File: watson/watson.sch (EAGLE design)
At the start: 37 parts

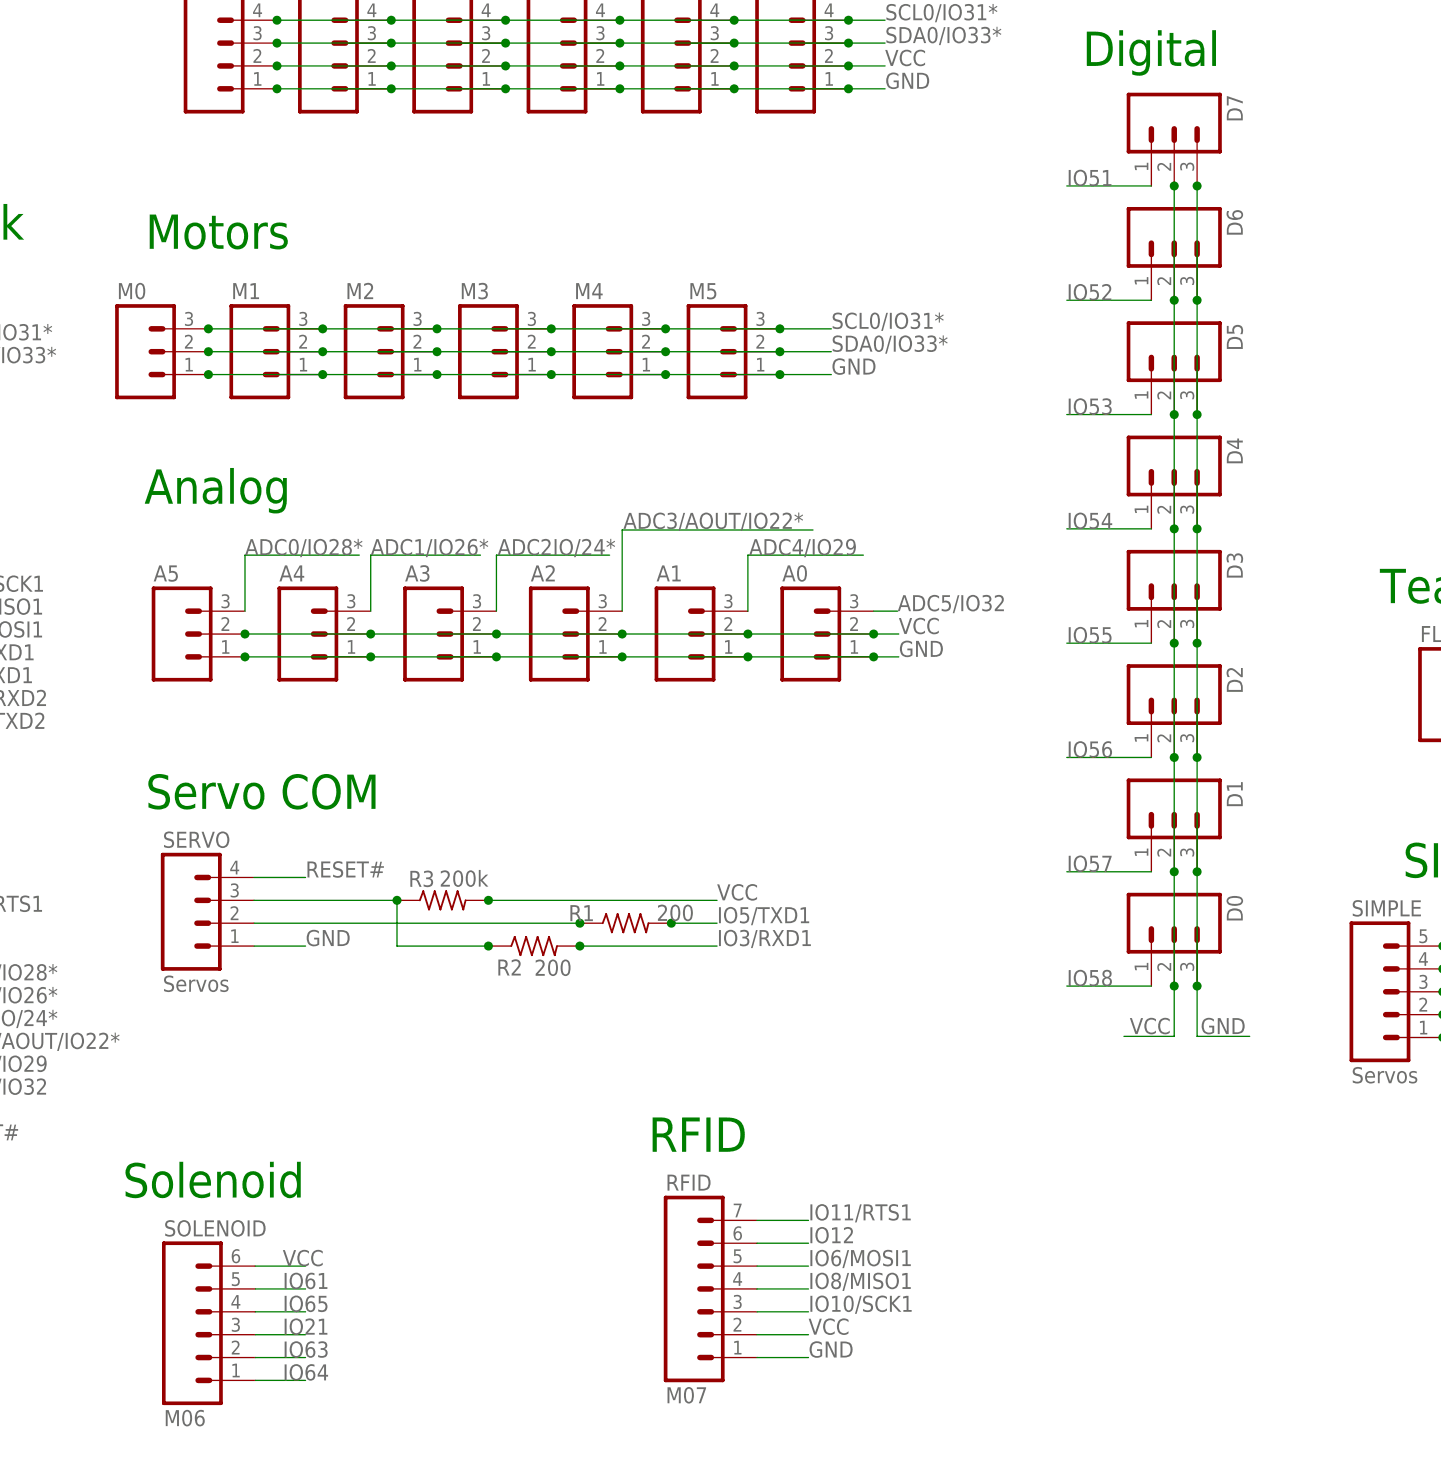
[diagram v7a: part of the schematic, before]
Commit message: Watson changes
holes aligned
silkscreen
gnd consistent
solenoid connected
etc.
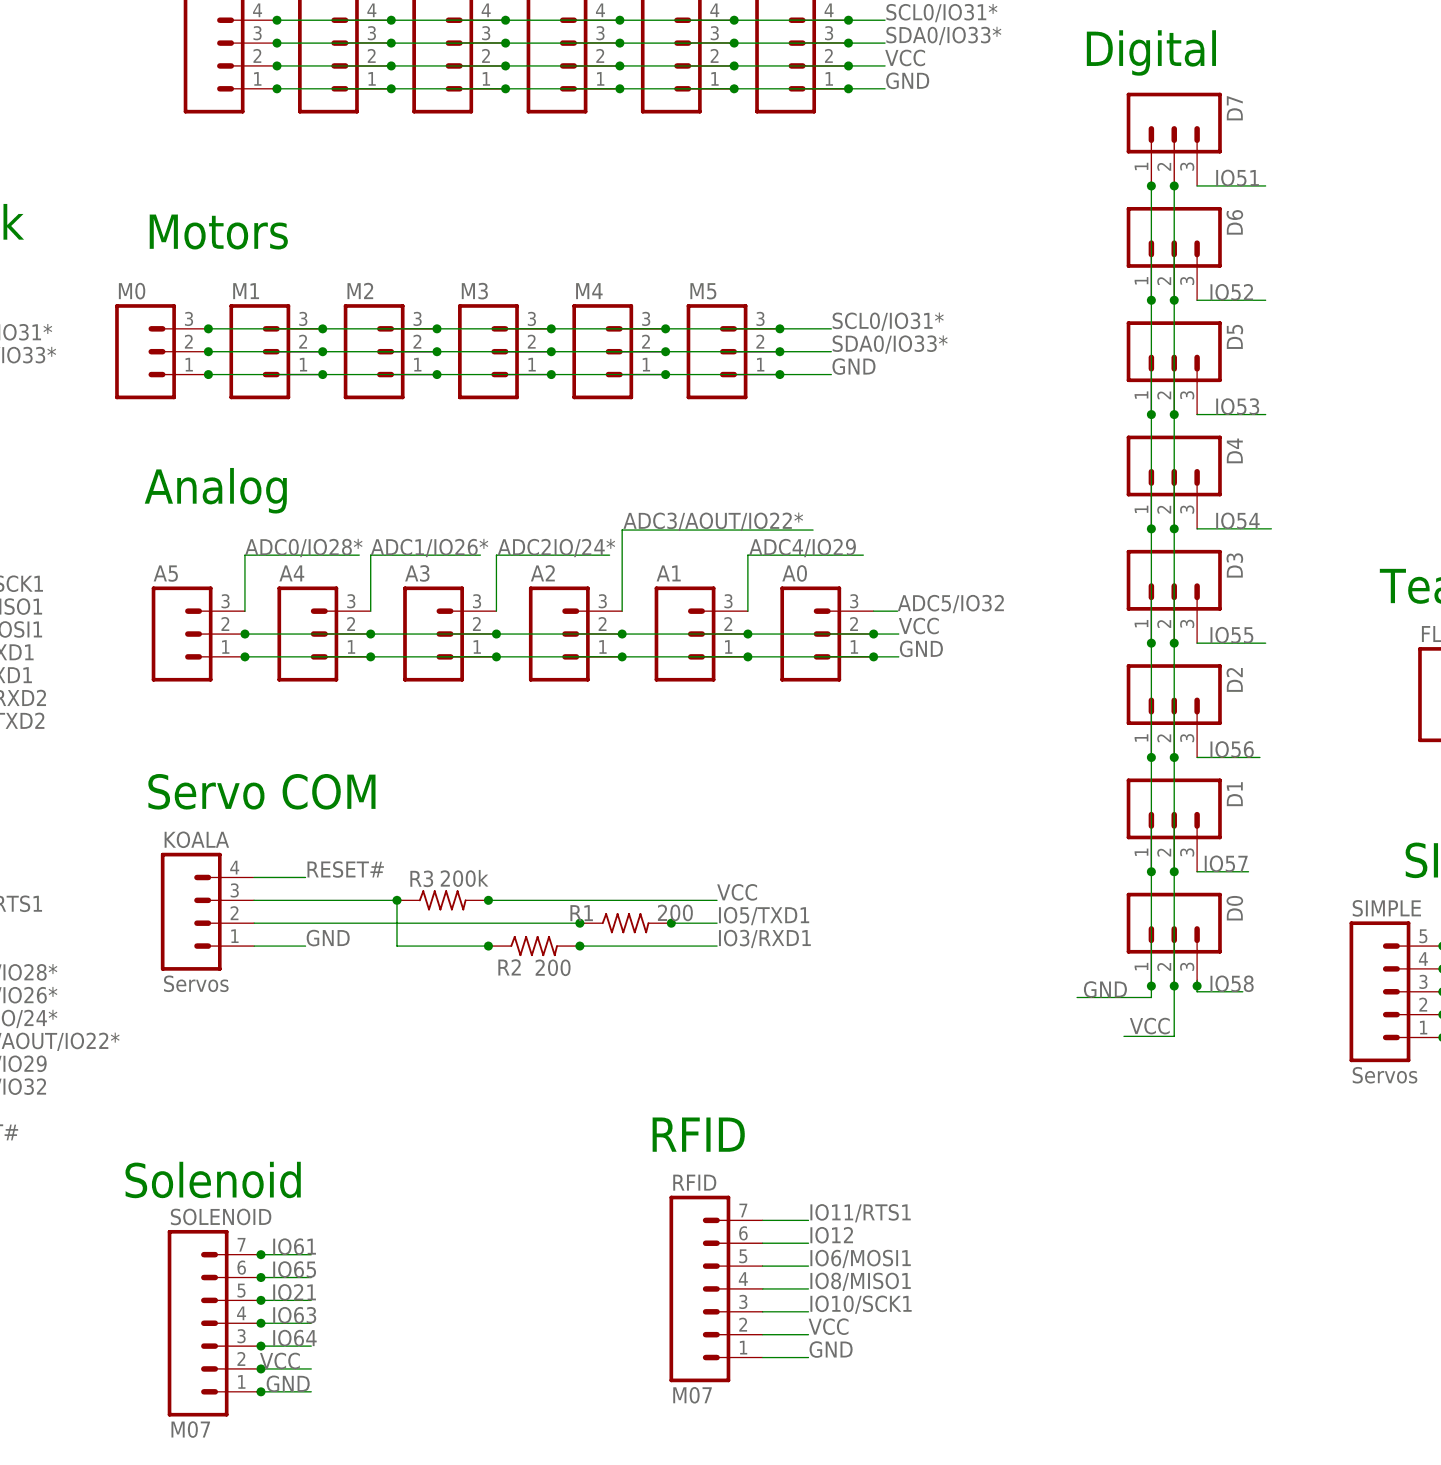
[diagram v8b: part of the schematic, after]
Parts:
- SOLENOID: value M06 -> M07; device pie:M06 -> pie:M07
- renumbered SERVO to KOALA
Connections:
- net GND: now also D0.1, D1.1, D2.1, D3.1, D4.1, D5.1, D6.1, D7.1, SOLENOID.1; no longer D0.3, D1.3, D2.3, D3.3, D4.3, D5.3, D6.3, D7.3
- net IO21: now also SOLENOID.5; no longer SOLENOID.3
- net IO51: now also D7.3; no longer D7.1
- net IO52: now also D6.3; no longer D6.1
- net IO53: now also D5.3; no longer D5.1
- net IO54: now also D4.3; no longer D4.1
- net IO55: now also D3.3; no longer D3.1
- net IO56: now also D2.3; no longer D2.1
- net IO57: now also D1.3; no longer D1.1
- net IO58: now also D0.3; no longer D0.1
- net IO61: now also SOLENOID.7; no longer SOLENOID.5
- net IO63: now also SOLENOID.4; no longer SOLENOID.2
- net IO64: now also SOLENOID.3; no longer SOLENOID.1
- net IO65: now also SOLENOID.6; no longer SOLENOID.4
- net VCC: now also SOLENOID.2; no longer SOLENOID.6
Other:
- moved on the sheet: RFID
